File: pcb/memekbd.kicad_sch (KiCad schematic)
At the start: 222 parts, among them J1 AudioJack4, J2 AudioJack4, SW1 SW_Push, SW10 SW_Push, SW11 SW_Push, SW12 SW_Push, SW13 SW_Push, SW14 SW_Push, SW15 SW_Push, SW16 SW_Push, SW17 SW_Push, SW18 SW_Push, SW19 SW_Push, SW2 SW_Push, SW20 SW_Push, SW21 SW_Push, SW22 SW_Push, SW23 SW_Push, SW24 SW_Push, SW25 SW_Push, SW26 SW_Push, SW27 SW_Push, SW28 SW_Push, SW29 SW_Push, SW3 SW_Push, SW30 SW_Push, SW31 SW_Push, SW32 SW_Push, SW33 SW_Push, SW34 SW_Push, SW35 SW_Push, SW36 SW_Push, SW37 SW_Push, SW38 SW_Push, SW39 SW_Push, SW4 SW_Push, SW40 SW_Push, SW41 SW_Push, SW42 SW_Push, SW43 SW_Push, SW44 SW_Push, SW45 SW_Push, SW46 SW_Push, SW47 SW_Push, SW48 SW_Push, SW5 SW_Push, SW6 SW_Push, SW7 SW_Push, SW8 SW_Push, SW9 SW_Push, U1 ProMicro, U2 ProMicro

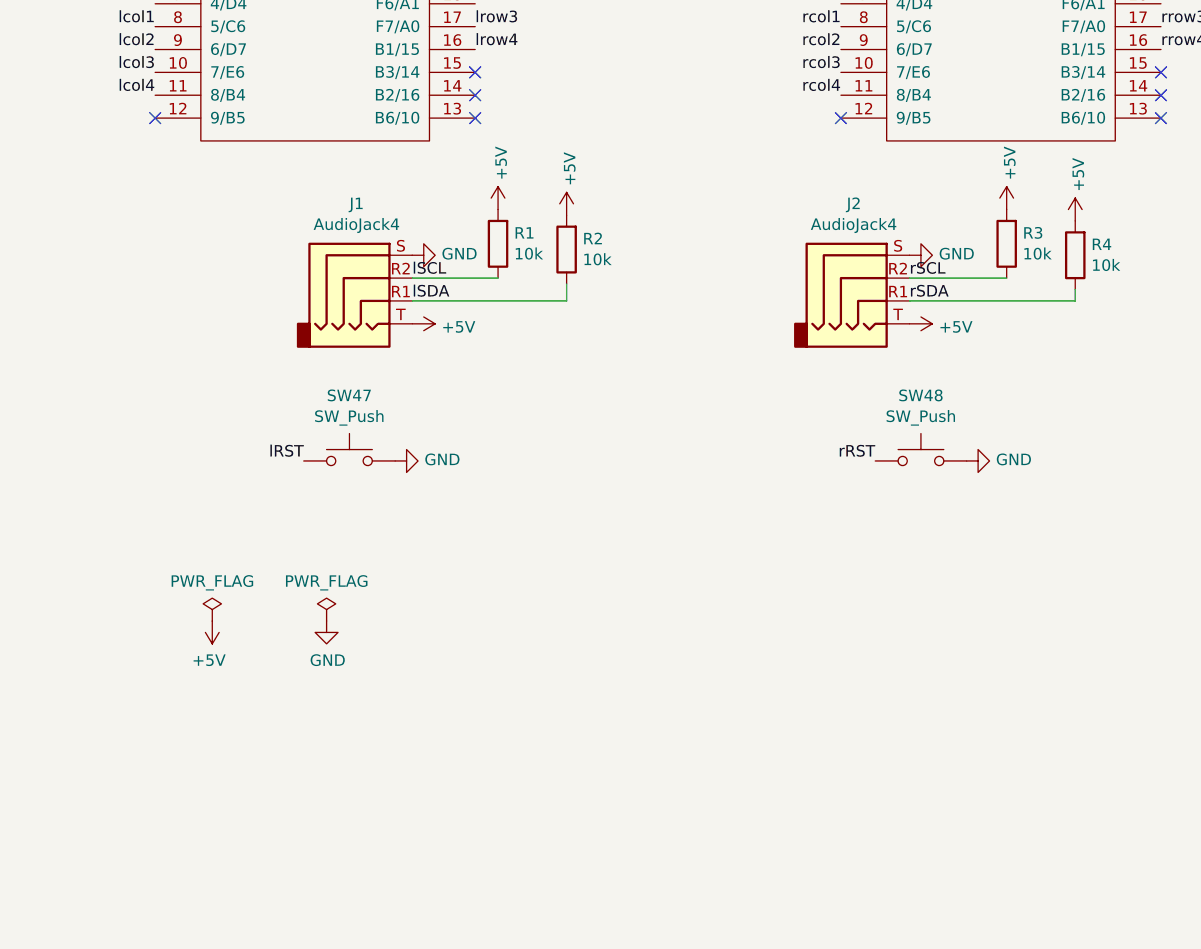
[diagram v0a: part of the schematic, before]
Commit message: Change schematic to use micro usb
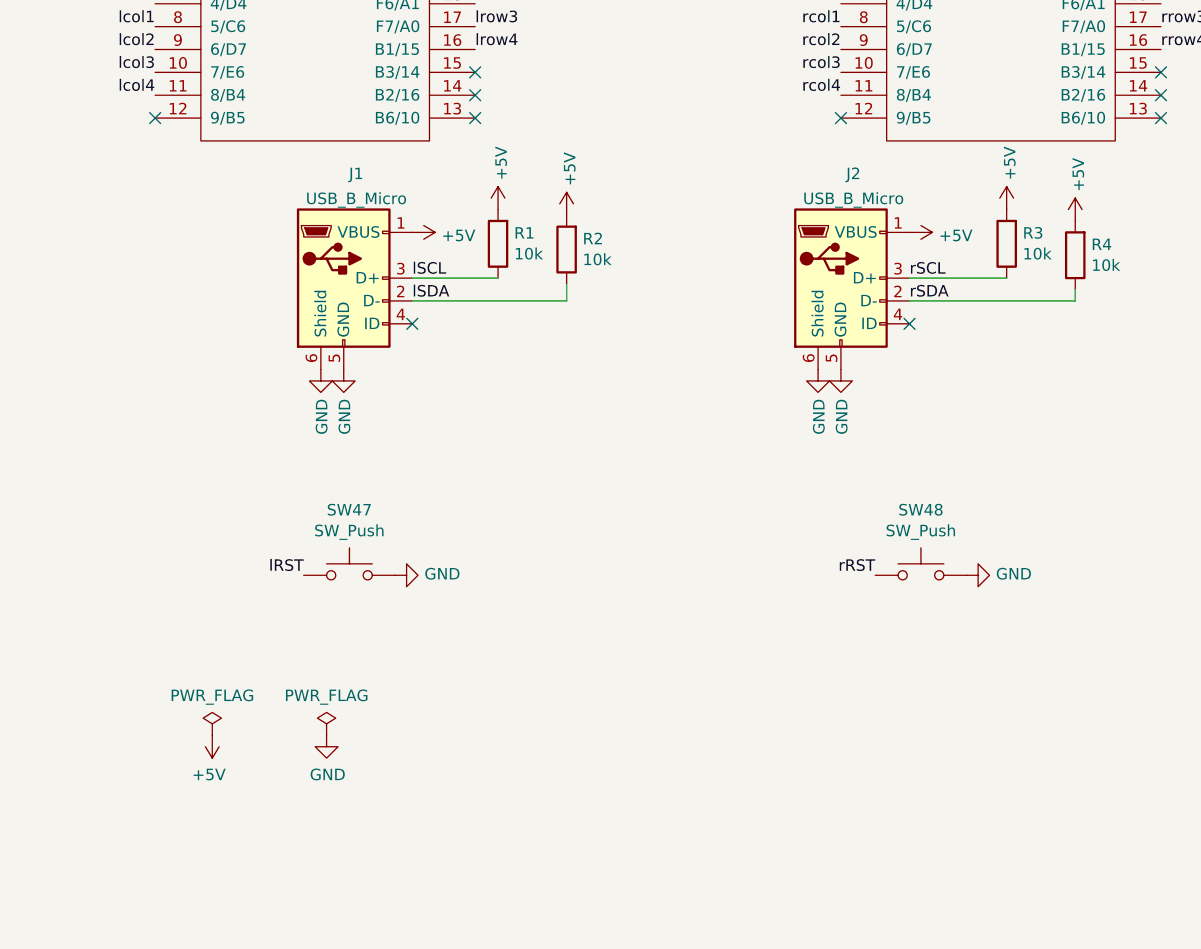
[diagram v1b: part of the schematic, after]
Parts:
- removed J1, J2: AudioJack4, Connector_Audio:Jack_3.5mm_PJ320D_Horizontal, symbol Connector:AudioJack4
- added J1, J2: USB_B_Micro, Connector_USB:USB_Micro-B_Wuerth_629105150521, symbol Connector:USB_B_Micro
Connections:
- net +5V: now also J1.1 (VBUS), J2.1 (VBUS)
- net GND: now also J1.5 (GND), J1.6 (Shield), J2.5 (GND), J2.6 (Shield)
- net lSCL: now also J1.3 (D+)
- net lSDA: now also J1.2 (D-)
- net rSCL: now also J2.3 (D+)
- net rSDA: now also J2.2 (D-)
- no-connect marks 14 -> 16
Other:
- moved on the sheet: SW47, SW48

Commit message: Update mounting hole footprint
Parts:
- H1, H14, H15, H16, H17, H2, H3, H4: footprint MountingHole:MountingHole_5.3mm_M5_ISO7380 -> MountingHole:MountingHole_5.3mm_M5_ISO7380_Pad
- H10, H11, H12, H13, H18, H19, H20, H21, H22, H23, H24, H25, H26, H5, H6, H7, H8, H9: footprint MountingHole:MountingHole_3.2mm_M3_ISO7380 -> MountingHole:MountingHole_3.2mm_M3_ISO7380_Pad

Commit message: Change location of keys.
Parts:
- removed H1, H14, H15, H16, H17, H2, H3, H4: MountingHole, MountingHole:MountingHole_5.3mm_M5_ISO7380_Pad, symbol Mechanical:MountingHole
- removed H10, H11, H12, H13, H18, H19, H20, H21, H22, H23, H24, H25, H26, H5, H6, H7, H8, H9: MountingHole, MountingHole:MountingHole_3.2mm_M3_ISO7380_Pad, symbol Mechanical:MountingHole
- added H1, H10, H11, H12, H13, H14, H15, H16, H2, H3, H4, H5, H6, H7, H8, H9: MountingHole_Pad, MountingHole:MountingHole_3.2mm_M3_ISO7380_Pad, symbol Mechanical:MountingHole_Pad
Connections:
- net GND: now also H1.1, H10.1, H11.1, H12.1, H13.1, H14.1, H15.1, H16.1, H2.1, H3.1, H4.1, H5.1, H6.1, H7.1, H8.1, H9.1
- net at LED5.4 (DIN): no longer R5.1
- net at R6.1: now also LED24.4 (DIN); no longer LED28.4 (DIN)
- net at LED1.4 (DIN): now also R5.1; no longer LED15.2 (DOUT)
- net at LED38.2 (DOUT): no longer LED24.4 (DIN)
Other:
- moved on the sheet: C10, C15, C28, C33, C38, C5, LED10, LED15, LED28, LED33, LED38, LED5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

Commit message: Work on reorg of keys
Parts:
- added C47, C48: 0.1uF, Capacitor_THT:C_Disc_D6.0mm_W2.5mm_P5.00mm, symbol Device:C_Small
- added D47, D48: 1N4148, Diode_THT:D_DO-35_SOD27_P7.62mm_Horizontal, symbol Diode:1N4148
- added LED47, LED48: YS-SK6812MINI-E, kbd:YS-SK6812MINI-E, symbol kbd:YS-SK6812MINI-E
- added SW49, SW50: SW_Push, kbd:CherryMX_Hotswap, symbol Switch:SW_Push
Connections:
- net +5V: now also C47.1, C48.1, LED47.1 (VDD), LED48.1 (VDD)
- net GND: now also C47.2, C48.2, LED47.3 (VSS), LED48.3 (VSS)
- net lcol0: now also SW5.1
- net lcol1: now also SW10.1; no longer SW5.1
- net lcol2: now also SW15.1; no longer SW10.1
- net lcol3: now also SW49.1; no longer SW15.1
- net lrow0: now also D1.1 (K), D11.1 (K), D16.1 (K), D20.1 (K), D6.1 (K); no longer D10.1 (K), D15.1 (K), D5.1 (K)
- net lrow1: now also D12.1 (K), D17.1 (K), D2.1 (K), D21.1 (K), D7.1 (K); no longer D1.1 (K), D11.1 (K), D16.1 (K), D20.1 (K), D6.1 (K)
- net lrow2: now also D13.1 (K), D18.1 (K), D22.1 (K), D3.1 (K), D8.1 (K); no longer D12.1 (K), D17.1 (K), D2.1 (K), D21.1 (K), D7.1 (K)
- net lrow3: now also D14.1 (K), D19.1 (K), D23.1 (K), D4.1 (K), D9.1 (K); no longer D13.1 (K), D18.1 (K), D22.1 (K), D3.1 (K), D8.1 (K)
- net lrow4: now also D10.1 (K), D15.1 (K), D5.1 (K), D47.1 (K); no longer D14.1 (K), D19.1 (K), D23.1 (K), D4.1 (K), D9.1 (K)
- net rcol0: now also SW28.1
- net rcol1: now also SW33.1; no longer SW28.1
- net rcol2: now also SW38.1; no longer SW33.1
- net rcol3: now also SW50.1; no longer SW38.1
- net rrow0: now also D24.1 (K), D29.1 (K), D34.1 (K), D39.1 (K), D43.1 (K); no longer D28.1 (K), D33.1 (K), D38.1 (K)
- net rrow1: now also D25.1 (K), D30.1 (K), D35.1 (K), D40.1 (K), D44.1 (K); no longer D24.1 (K), D29.1 (K), D34.1 (K), D39.1 (K), D43.1 (K)
- net rrow2: now also D26.1 (K), D31.1 (K), D36.1 (K), D41.1 (K), D45.1 (K); no longer D25.1 (K), D30.1 (K), D35.1 (K), D40.1 (K), D44.1 (K)
- net rrow3: now also D27.1 (K), D32.1 (K), D37.1 (K), D42.1 (K), D46.1 (K); no longer D26.1 (K), D31.1 (K), D36.1 (K), D41.1 (K), D45.1 (K)
- net rrow4: now also D28.1 (K), D33.1 (K), D38.1 (K), D48.1 (K); no longer D27.1 (K), D32.1 (K), D37.1 (K), D42.1 (K), D46.1 (K)
- net at LED5.4 (DIN): now also LED23.2 (DOUT)
- net at LED15.2 (DOUT): now also LED47.4 (DIN)
- net at LED46.2 (DOUT): now also LED28.4 (DIN)
- net at LED38.2 (DOUT): now also LED48.4 (DIN)
- new net: D47.2 (A), SW49.2
- new net: D48.2 (A), SW50.2
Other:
- moved on the sheet: C10, C15, C28, C33, C38, C5, D1, D10, D11, D12, D13, D14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
